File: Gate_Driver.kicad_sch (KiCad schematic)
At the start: 27 parts, among them U1 DRV8323RSRGZR

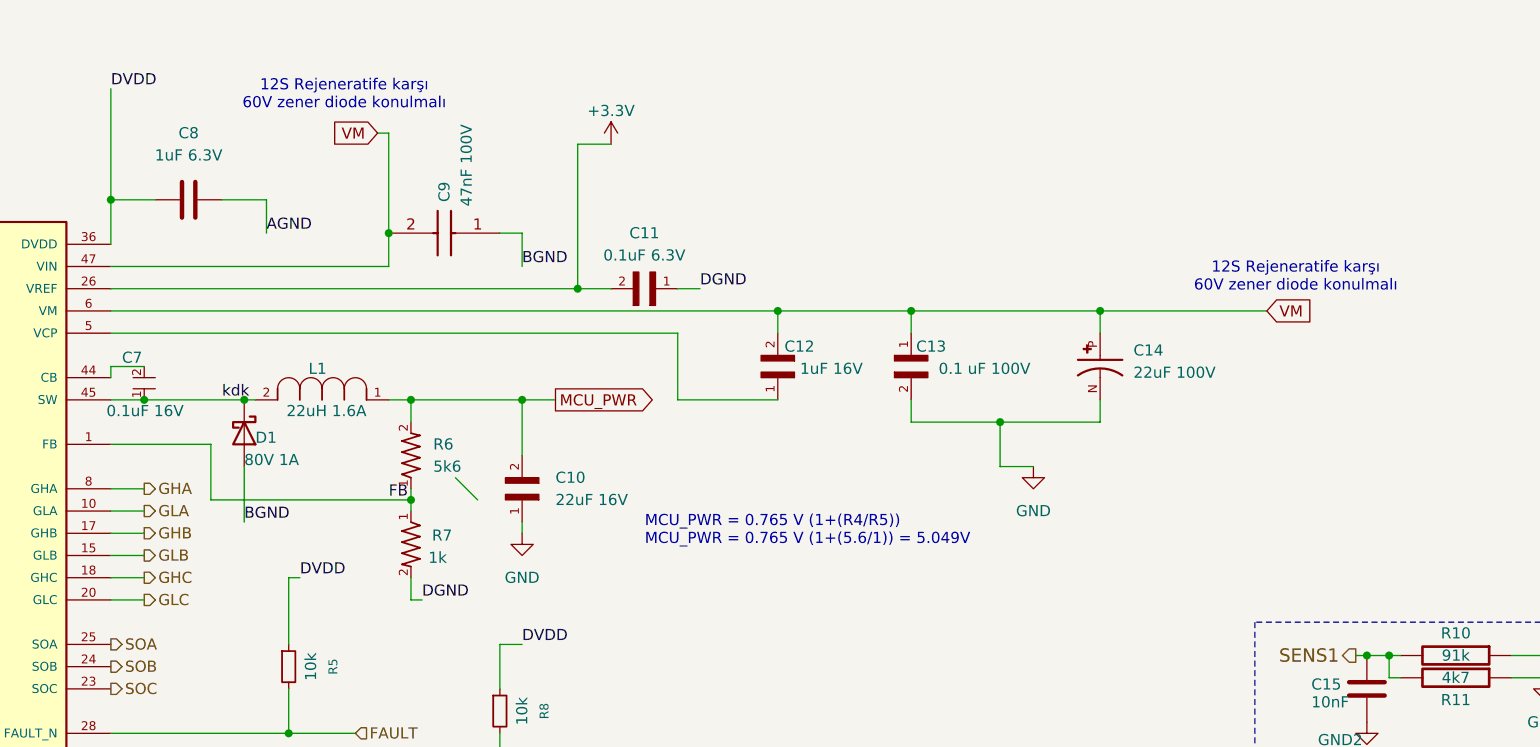
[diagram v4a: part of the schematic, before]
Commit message: for LCSC components the layout/footprints changed. Previous commit for ekom/direncnet components.
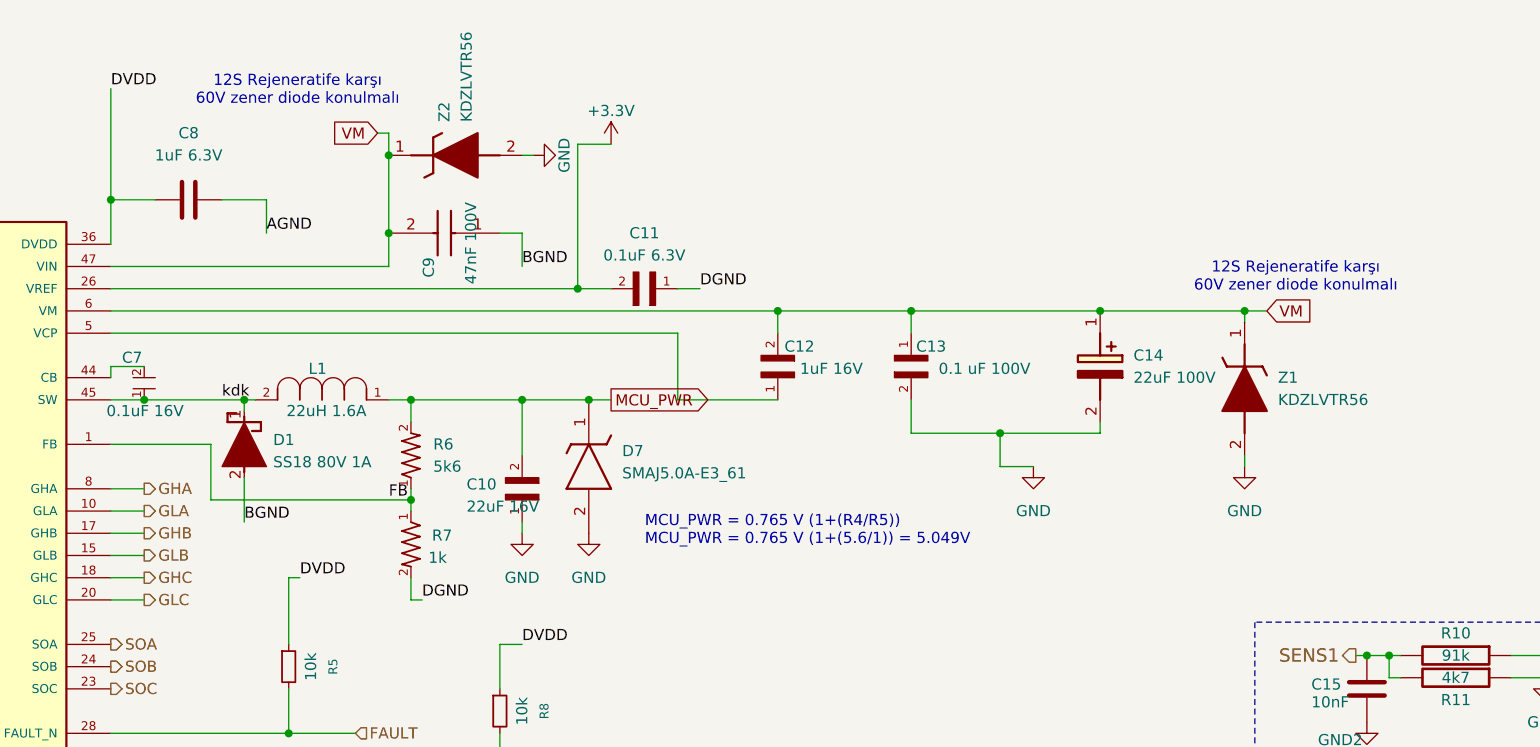
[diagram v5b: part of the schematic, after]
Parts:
- removed C14: 22uF 100V, ECA2AM220B:CAPPRD500W50D630H1120, symbol ECA2AM220B:ECA2AM220B
- removed D1: 80V 1A, Diode_SMD:D_SMA, symbol Diode:SS18
- added C14: 22uF 100V, CAPPRD250W50D655H1250, symbol 100YXJ22M6_3X11:100YXJ22M6.3X11
- added D1: SS18 80V 1A, DIOM5227X270N, symbol SS18:SS18
- added D7: SMAJ5.0A-E3_61, DIOM5127X229N, symbol SMAJ5_0A-E3_61:SMAJ5.0A-E3_61
- added Z1, Z2: KDZLVTR56, KDZLVTR56, symbol KDZLVTR56:KDZLVTR56
- C10, C6, C9: footprint Capacitor_SMD:C_0805_2012Metric_Pad1.18x1.45mm_HandSolder -> Capacitor_SMD:C_0603_1608Metric_Pad1.08x0.95mm_HandSolder
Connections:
- net GND: now also C14.2 (-), D1.2 (A), D7.2 (A), Z1.2 (A), Z2.2 (A)
- net MCU_PWR: now also D7.1 (K)
- net VM: now also C14.1 (+), Z1.1 (K), Z2.1 (K)
- net kdk: now also D1.1 (K)
